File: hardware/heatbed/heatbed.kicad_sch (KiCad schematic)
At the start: 6 parts, among them J1 Conn_01x01, J2 Conn_01x01

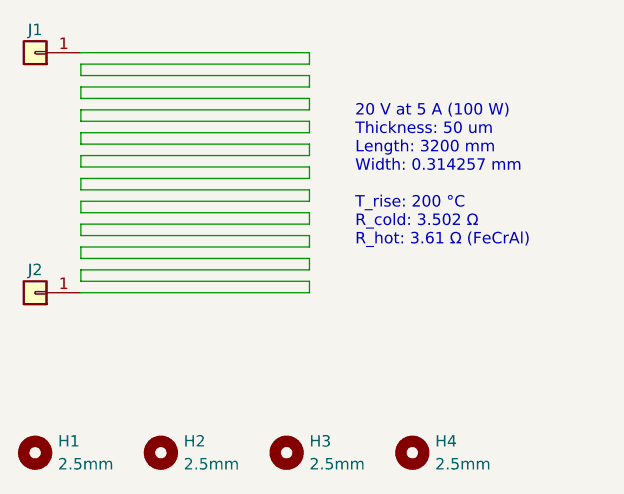
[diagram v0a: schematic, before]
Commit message: finish board and prod/case files
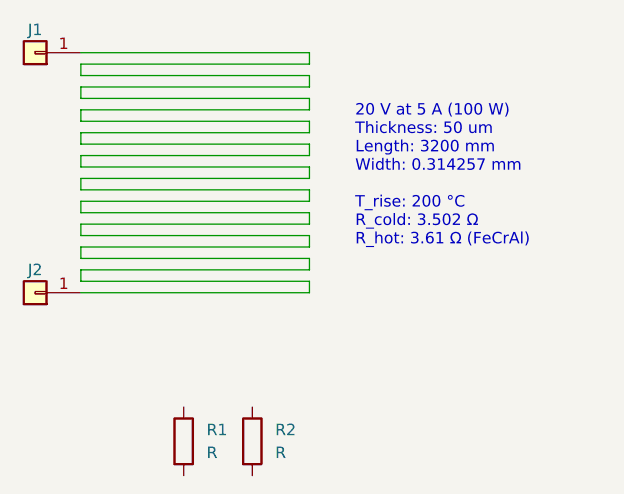
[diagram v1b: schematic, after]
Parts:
- removed H1, H2, H3, H4: 2.5mm, MountingHole:MountingHole_2.5mm, symbol Mechanical:MountingHole
- added R1, R2: R, Resistor_SMD:R_0805_2012Metric, symbol Device:R
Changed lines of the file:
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@@
-	)
-	(symbol
-		(lib_id "Mechanical:MountingHole")
-		(at 149.86 118.11 0)
-		(unit 1)
-		(exclude_from_sim no)
-		(in_bom no)
-		(on_board yes)
-		(dnp no)
-		(fields_autoplaced yes)
-		(property "Reference" "H4"
-			(at 152.4 116.84 0)
-			(effects
-				(font
-					(size 1.27 1.27)
-				)
-				(justify left)
-			)
-		)
-		(property "Value" "2.5mm"
-			(at 152.4 119.38 0)
-			(effects
-				(font
-					(size 1.27 1.27)
-				)
-				(justify left)
-			)
-		)
-		(property "Footprint" "MountingHole:MountingHole_2.5mm"
-			(at 149.86 118.11 0)
-			(effects
-				(font
-					(size 1.27 1.27)
-				)
-				(hide yes)
-			)
-		)
-		(property "Datasheet" "~"
-			(at 149.86 118.11 0)
-			(effects
-				(font
-					(size 1.27 1.27)
-				)
-				(hide yes)
-			)
-		)
-		(property "Description" ""
-			(at 149.86 118.11 0)
-			(effects
-				(font
-					(size 1.27 1.27)
-				)
-			)
-		)
-		(instances
-			(project "heatbed"
-				(path "/96c94e77-9bbd-4951-87d6-275abac027c2"
-					(reference "H4")
-					(unit 1)
-				)
-			)
-		)
 	)
 	(symbol
@@
 	)
 	(symbol
-		(lib_id "Mechanical:MountingHole")
-		(at 107.95 118.11 0)
+		(lib_id "Device:R")
+		(at 132.08 116.84 0)
 		(unit 1)
 		(exclude_from_sim no)
-		(in_bom no)
+		(in_bom yes)
 		(on_board yes)
 		(dnp no)
 		(fields_autoplaced yes)
-		(property "Reference" "H1"
-			(at 110.49 116.84 0)
+		(property "Reference" "R2"
+			(at 134.62 115.5699 0)
 			(effects
 				(font
@@
 			)
 		)
-		(property "Value" "2.5mm"
-			(at 110.49 119.38 0)
+		(property "Value" "R"
+			(at 134.62 118.1099 0)
 			(effects
 				(font
@@
 			)
 		)
-		(property "Footprint" "MountingHole:MountingHole_2.5mm"
-			(at 107.95 118.11 0)
+		(property "Footprint" "Resistor_SMD:R_0805_2012Metric"
+			(at 130.302 116.84 90)
 			(effects
 				(font
@@
 		)
 		(property "Datasheet" "~"
-			(at 107.95 118.11 0)
+			(at 132.08 116.84 0)
 			(effects
 				(font
@@
 			)
 		)
-		(property "Description" ""
-			(at 107.95 118.11 0)
+		(property "Description" "Resistor"
+			(at 132.08 116.84 0)
 			(effects
 				(font
 					(size 1.27 1.27)
 				)
+				(hide yes)
 			)
+		)
+		(pin "1"
+		)
+		(pin "2"
 		)
 		(instances
 			(project "heatbed"
 				(path "/96c94e77-9bbd-4951-87d6-275abac027c2"
-					(reference "H1")
+					(reference "R2")
 					(unit 1)
 				)
@@
 	)
 	(symbol
-		(lib_id "Mechanical:MountingHole")
-		(at 121.92 118.11 0)
+		(lib_id "Device:R")
+		(at 124.46 116.84 0)
 		(unit 1)
 		(exclude_from_sim no)
-		(in_bom no)
+		(in_bom yes)
 		(on_board yes)
 		(dnp no)
 		(fields_autoplaced yes)
-		(property "Reference" "H2"
-			(at 124.46 116.84 0)
+		(property "Reference" "R1"
+			(at 127 115.5699 0)
 			(effects
 				(font
@@
 			)
 		)
-		(property "Value" "2.5mm"
-			(at 124.46 119.38 0)
+		(property "Value" "R"
+			(at 127 118.1099 0)
 			(effects
 				(font
@@
 			)
 		)
-		(property "Footprint" "MountingHole:MountingHole_2.5mm"
-			(at 121.92 118.11 0)
+		(property "Footprint" "Resistor_SMD:R_0805_2012Metric"
+			(at 122.682 116.84 90)
 			(effects
 				(font
@@
 		)
 		(property "Datasheet" "~"
-			(at 121.92 118.11 0)
+			(at 124.46 116.84 0)
 			(effects
 				(font
@@
 			)
 		)
-		(property "Description" ""
-			(at 121.92 118.11 0)
-			(effects
-				(font
-					(size 1.27 1.27)
-				)
-			)
-		)
-		(instances
-			(project "heatbed"
-				(path "/96c94e77-9bbd-4951-87d6-275abac027c2"
-					(reference "H2")
-					(unit 1)
-				)
-			)
-		)
-	)
-	(symbol
-		(lib_id "Mechanical:MountingHole")
-		(at 135.89 118.11 0)
-		(unit 1)
-		(exclude_from_sim no)
-		(in_bom no)
-		(on_board yes)
-		(dnp no)
-		(fields_autoplaced yes)
-		(property "Reference" "H3"
-			(at 138.43 116.84 0)
-			(effects
-				(font
-					(size 1.27 1.27)
-				)
-				(justify left)
-			)
-		)
-		(property "Value" "2.5mm"
-			(at 138.43 119.38 0)
-			(effects
-				(font
-					(size 1.27 1.27)
-				)
-				(justify left)
-			)
-		)
-		(property "Footprint" "MountingHole:MountingHole_2.5mm"
-			(at 135.89 118.11 0)
+		(property "Description" "Resistor"
+			(at 124.46 116.84 0)
 			(effects
 				(font
@@
 			)
 		)
-		(property "Datasheet" "~"
-			(at 135.89 118.11 0)
-			(effects
-				(font
-					(size 1.27 1.27)
-				)
-				(hide yes)
-			)
+		(pin "1"
 		)
-		(property "Description" ""
-			(at 135.89 118.11 0)
-			(effects
-				(font
-					(size 1.27 1.27)
-				)
-			)
+		(pin "2"
 		)
 		(instances
-			(project "heatbed"
+			(project ""
 				(path "/96c94e77-9bbd-4951-87d6-275abac027c2"
-					(reference "H3")
+					(reference "R1")
 					(unit 1)
 				)

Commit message: add heatbed image
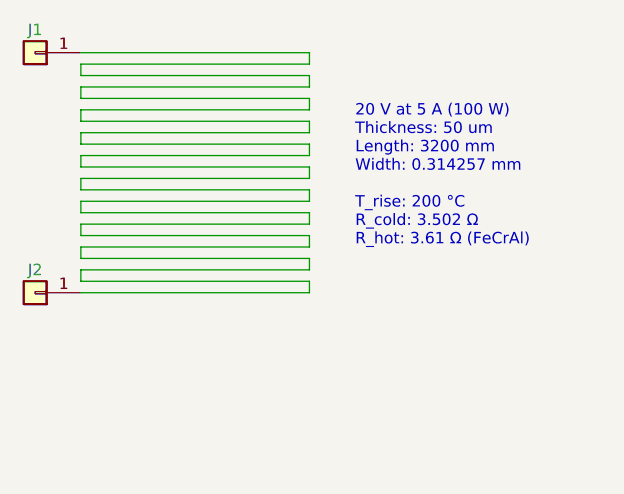
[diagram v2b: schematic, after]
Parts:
- removed R1, R2: R, Resistor_SMD:R_0805_2012Metric, symbol Device:R
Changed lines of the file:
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@@
-		)
-	)
-	(symbol
-		(lib_id "Device:R")
-		(at 132.08 116.84 0)
-		(unit 1)
-		(exclude_from_sim no)
-		(in_bom yes)
-		(on_board yes)
-		(dnp no)
-		(fields_autoplaced yes)
-		(property "Reference" "R2"
-			(at 134.62 115.5699 0)
-			(effects
-				(font
-					(size 1.27 1.27)
-				)
-				(justify left)
-			)
-		)
-		(property "Value" "R"
-			(at 134.62 118.1099 0)
-			(effects
-				(font
-					(size 1.27 1.27)
-				)
-				(justify left)
-			)
-		)
-		(property "Footprint" "Resistor_SMD:R_0805_2012Metric"
-			(at 130.302 116.84 90)
-			(effects
-				(font
-					(size 1.27 1.27)
-				)
-				(hide yes)
-			)
-		)
-		(property "Datasheet" "~"
-			(at 132.08 116.84 0)
-			(effects
-				(font
-					(size 1.27 1.27)
-				)
-				(hide yes)
-			)
-		)
-		(property "Description" "Resistor"
-			(at 132.08 116.84 0)
-			(effects
-				(font
-					(size 1.27 1.27)
-				)
-				(hide yes)
-			)
-		)
-		(pin "1"
-		)
-		(pin "2"
-		)
-		(instances
-			(project "heatbed"
-				(path "/96c94e77-9bbd-4951-87d6-275abac027c2"
-					(reference "R2")
-					(unit 1)
-				)
-			)
-		)
-	)
-	(symbol
-		(lib_id "Device:R")
-		(at 124.46 116.84 0)
-		(unit 1)
-		(exclude_from_sim no)
-		(in_bom yes)
-		(on_board yes)
-		(dnp no)
-		(fields_autoplaced yes)
-		(property "Reference" "R1"
-			(at 127 115.5699 0)
-			(effects
-				(font
-					(size 1.27 1.27)
-				)
-				(justify left)
-			)
-		)
-		(property "Value" "R"
-			(at 127 118.1099 0)
-			(effects
-				(font
-					(size 1.27 1.27)
-				)
-				(justify left)
-			)
-		)
-		(property "Footprint" "Resistor_SMD:R_0805_2012Metric"
-			(at 122.682 116.84 90)
-			(effects
-				(font
-					(size 1.27 1.27)
-				)
-				(hide yes)
-			)
-		)
-		(property "Datasheet" "~"
-			(at 124.46 116.84 0)
-			(effects
-				(font
-					(size 1.27 1.27)
-				)
-				(hide yes)
-			)
-		)
-		(property "Description" "Resistor"
-			(at 124.46 116.84 0)
-			(effects
-				(font
-					(size 1.27 1.27)
-				)
-				(hide yes)
-			)
-		)
-		(pin "1"
-		)
-		(pin "2"
-		)
-		(instances
-			(project ""
-				(path "/96c94e77-9bbd-4951-87d6-275abac027c2"
-					(reference "R1")
-					(unit 1)
-				)
-			)
 		)
 	)

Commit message: fixed via sizing
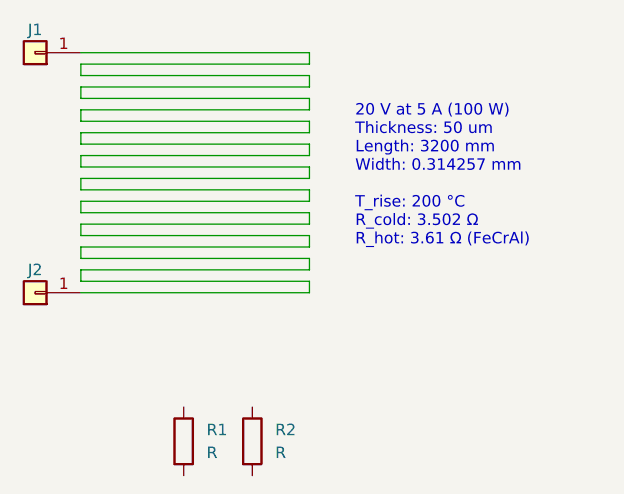
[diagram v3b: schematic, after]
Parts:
- added R1, R2: R, Resistor_SMD:R_0805_2012Metric, symbol Device:R
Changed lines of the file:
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@@
+		)
+	)
+	(symbol
+		(lib_id "Device:R")
+		(at 132.08 116.84 0)
+		(unit 1)
+		(exclude_from_sim no)
+		(in_bom yes)
+		(on_board yes)
+		(dnp no)
+		(fields_autoplaced yes)
+		(property "Reference" "R2"
+			(at 134.62 115.5699 0)
+			(effects
+				(font
+					(size 1.27 1.27)
+				)
+				(justify left)
+			)
+		)
+		(property "Value" "R"
+			(at 134.62 118.1099 0)
+			(effects
+				(font
+					(size 1.27 1.27)
+				)
+				(justify left)
+			)
+		)
+		(property "Footprint" "Resistor_SMD:R_0805_2012Metric"
+			(at 130.302 116.84 90)
+			(effects
+				(font
+					(size 1.27 1.27)
+				)
+				(hide yes)
+			)
+		)
+		(property "Datasheet" "~"
+			(at 132.08 116.84 0)
+			(effects
+				(font
+					(size 1.27 1.27)
+				)
+				(hide yes)
+			)
+		)
+		(property "Description" "Resistor"
+			(at 132.08 116.84 0)
+			(effects
+				(font
+					(size 1.27 1.27)
+				)
+				(hide yes)
+			)
+		)
+		(pin "1"
+		)
+		(pin "2"
+		)
+		(instances
+			(project "heatbed"
+				(path "/96c94e77-9bbd-4951-87d6-275abac027c2"
+					(reference "R2")
+					(unit 1)
+				)
+			)
+		)
+	)
+	(symbol
+		(lib_id "Device:R")
+		(at 124.46 116.84 0)
+		(unit 1)
+		(exclude_from_sim no)
+		(in_bom yes)
+		(on_board yes)
+		(dnp no)
+		(fields_autoplaced yes)
+		(property "Reference" "R1"
+			(at 127 115.5699 0)
+			(effects
+				(font
+					(size 1.27 1.27)
+				)
+				(justify left)
+			)
+		)
+		(property "Value" "R"
+			(at 127 118.1099 0)
+			(effects
+				(font
+					(size 1.27 1.27)
+				)
+				(justify left)
+			)
+		)
+		(property "Footprint" "Resistor_SMD:R_0805_2012Metric"
+			(at 122.682 116.84 90)
+			(effects
+				(font
+					(size 1.27 1.27)
+				)
+				(hide yes)
+			)
+		)
+		(property "Datasheet" "~"
+			(at 124.46 116.84 0)
+			(effects
+				(font
+					(size 1.27 1.27)
+				)
+				(hide yes)
+			)
+		)
+		(property "Description" "Resistor"
+			(at 124.46 116.84 0)
+			(effects
+				(font
+					(size 1.27 1.27)
+				)
+				(hide yes)
+			)
+		)
+		(pin "1"
+		)
+		(pin "2"
+		)
+		(instances
+			(project ""
+				(path "/96c94e77-9bbd-4951-87d6-275abac027c2"
+					(reference "R1")
+					(unit 1)
+				)
+			)
 		)
 	)
